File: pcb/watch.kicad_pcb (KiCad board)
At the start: 2 copper layers, 25.4 x 25.4 mm, 27 parts, among them SW1 EVP-AA202K, SW2 EVP-AA202K, U1 ATtiny402-SS

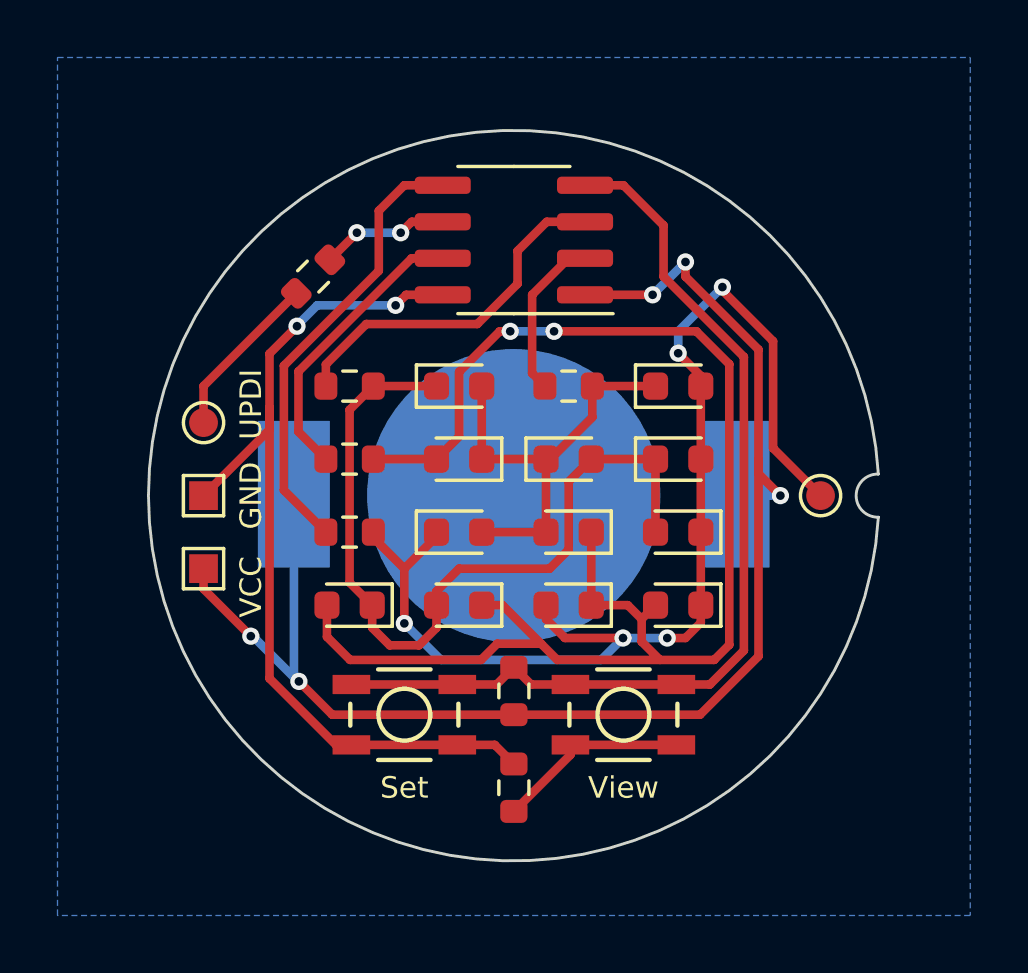
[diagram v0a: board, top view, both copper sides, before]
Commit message: Use a CR2032 instead of a CR1216
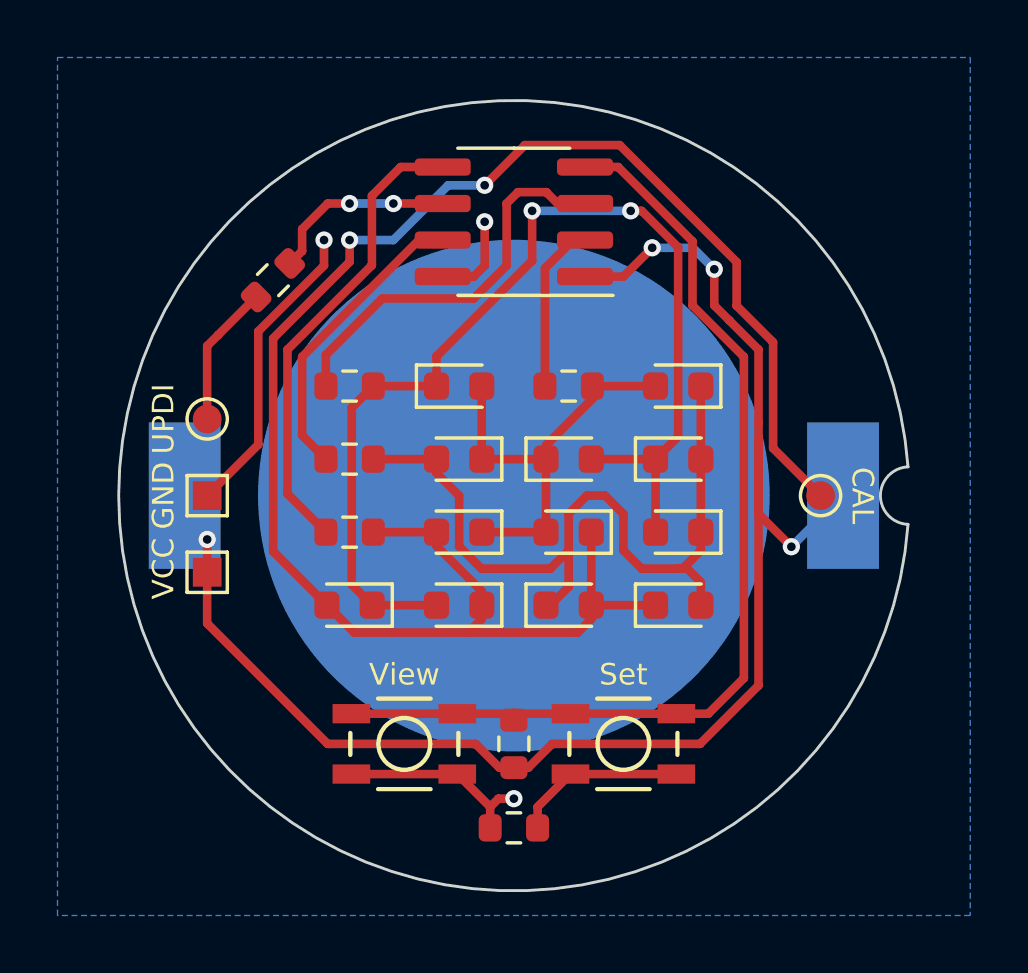
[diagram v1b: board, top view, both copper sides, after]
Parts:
- BT1: value BK-916-TR -> BAT-HLD-001-TR; footprint Battery Holder:BAT_BK-916-TR -> Battery Holder:BAT_BAT-HLD-001-TR
- moved D11 12.5 mm to (57.8, 67.3), turned to 180 degrees
- moved D9 12.5 mm to (69.2, 62.2), turned to 0 degrees
- moved D7 9.16 mm to (61.6, 64.8), turned to 180 degrees
- moved D10 8.03 mm to (69.2, 64.8)
- moved D12 8.03 mm to (61.6, 67.3)
- moved D4 6.35 mm to (69.2, 59.7)
- moved D8 3.81 mm to (65.4, 64.8), turned to 180 degrees
- moved R5 1.84 mm to (63.5, 72.1)
- moved R7 1.40 mm to (55.1, 56.0)
- moved R6 1.40 mm to (63.5, 75.1), turned to 180 degrees
- moved SW1 1.02 mm to (59.7, 72.1)
- moved SW2 1.02 mm to (67.3, 72.1)
- moved U1 0.63 mm to (63.5, 54.0)
- moved TP1 0.18 mm to (52.8, 60.8)
- moved TP3 0.18 mm to (52.8, 66.2)
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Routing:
- net Net-(D1-Pad1): track 51.4 -> 28.0 mm, vias 2 -> 0
- net Net-(D1-Pad2): track 41.5 -> 62.0 mm, vias 5 -> 2
- net GND: track 31.9 -> 20.7 mm, vias 2 -> 3
- net Net-(D10-Pad2): track 28.7 -> 38.2 mm, vias 0 -> 2
- net Net-(R7-Pad1): track 4.47 -> 6.63 mm
- net Net-(R4-Pad1): track 12.5 -> 13.9 mm
- net Net-(R5-Pad2): track 33.9 -> 35.2 mm
- net +3.3V: track 51.2 -> 52.4 mm, vias 5 -> 4
- net Net-(R7-Pad2): track 5.83 -> 4.95 mm
- net Net-(R6-Pad1): track 6.81 -> 6.03 mm
- net Net-(R1-Pad1): track 15.7 -> 16.3 mm
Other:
- board size 25.4 x 25.4 mm -> 27.5 x 27.5 mm
- board text added: "CAL"
- board text added: "rev 2.0"

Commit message: Modify PCB to work with more fabrication services Also rotate the alignment pin
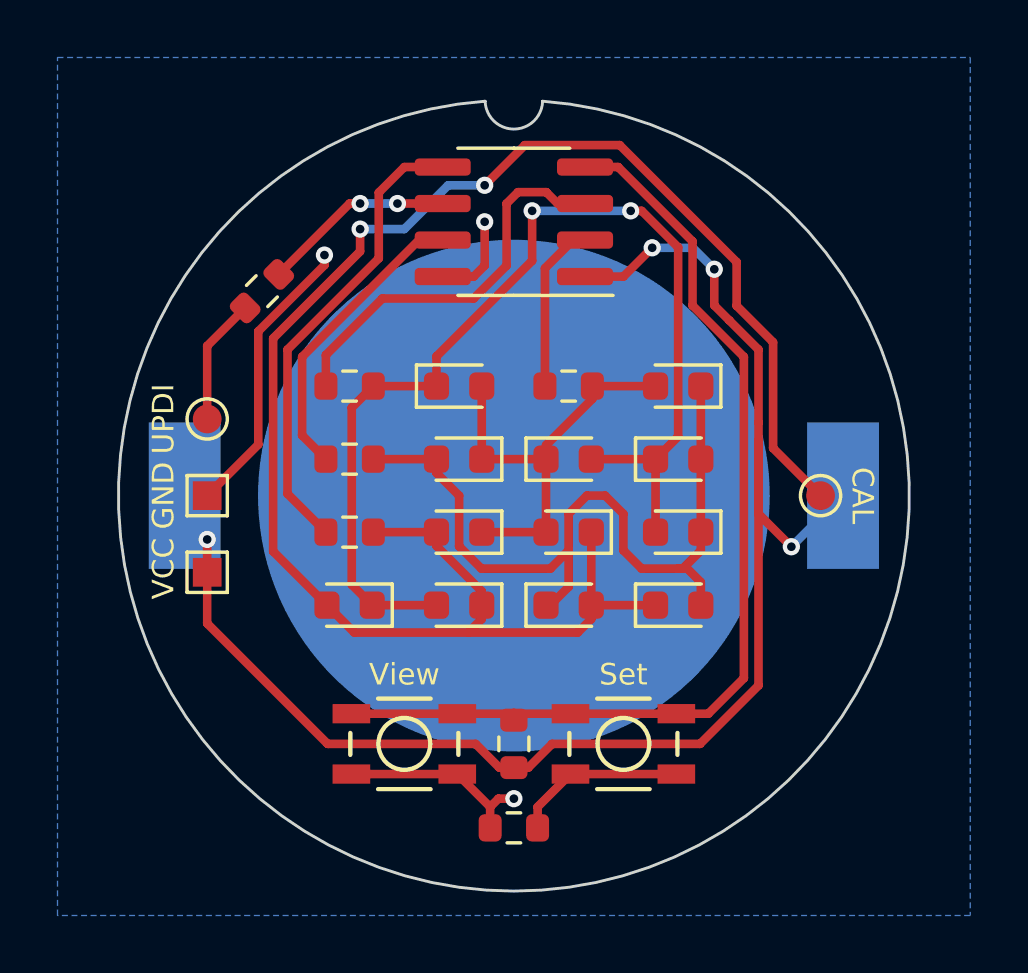
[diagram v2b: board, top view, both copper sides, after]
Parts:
- moved R7 0.54 mm to (54.7, 56.4)
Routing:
- net Net-(R7-Pad2): track 4.95 -> 4.41 mm
- net GND: track 20.7 -> 20.2 mm
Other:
- outline, holes or cut-outs redrawn
- board text added: "rev 2.1"
- board text removed: "rev 2.0"
